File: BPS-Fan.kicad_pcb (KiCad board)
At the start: 2 copper layers, 57.3 x 82.1 mm, 37 parts, among them J1 LDRBRDConn, J10 FAN9, J11 FAN10, J12 FAN11, J13 FAN12, J2 FAN1, J3 FAN2, J4 FAN3, J5 FAN4, J6 FAN5, J7 FAN6, J8 FAN7, J9 FAN8, Q1 BUK9M23-80E, Q2 BUK9M23-80E, Q3 BUK9M23-80E, Q4 BUK9M23-80E

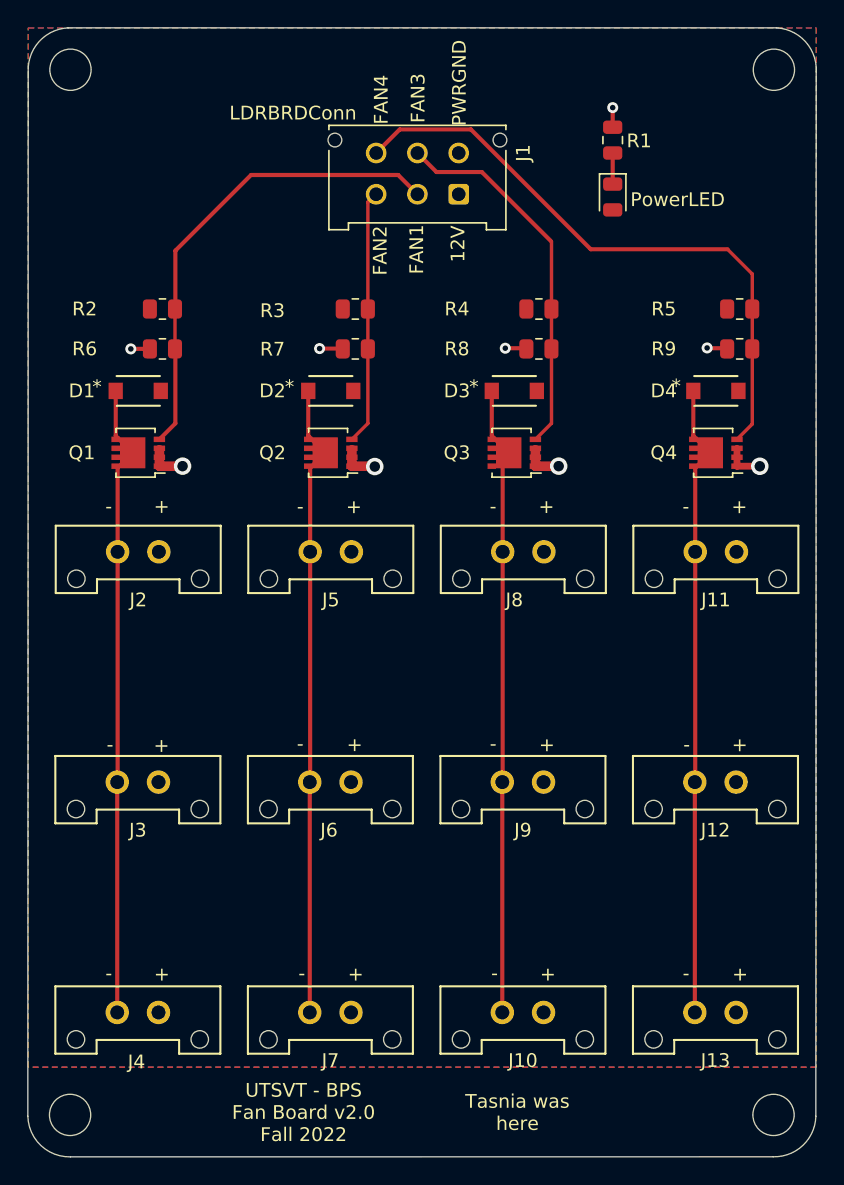
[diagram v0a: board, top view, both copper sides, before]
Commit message: updated BOM and data sheet in schematic
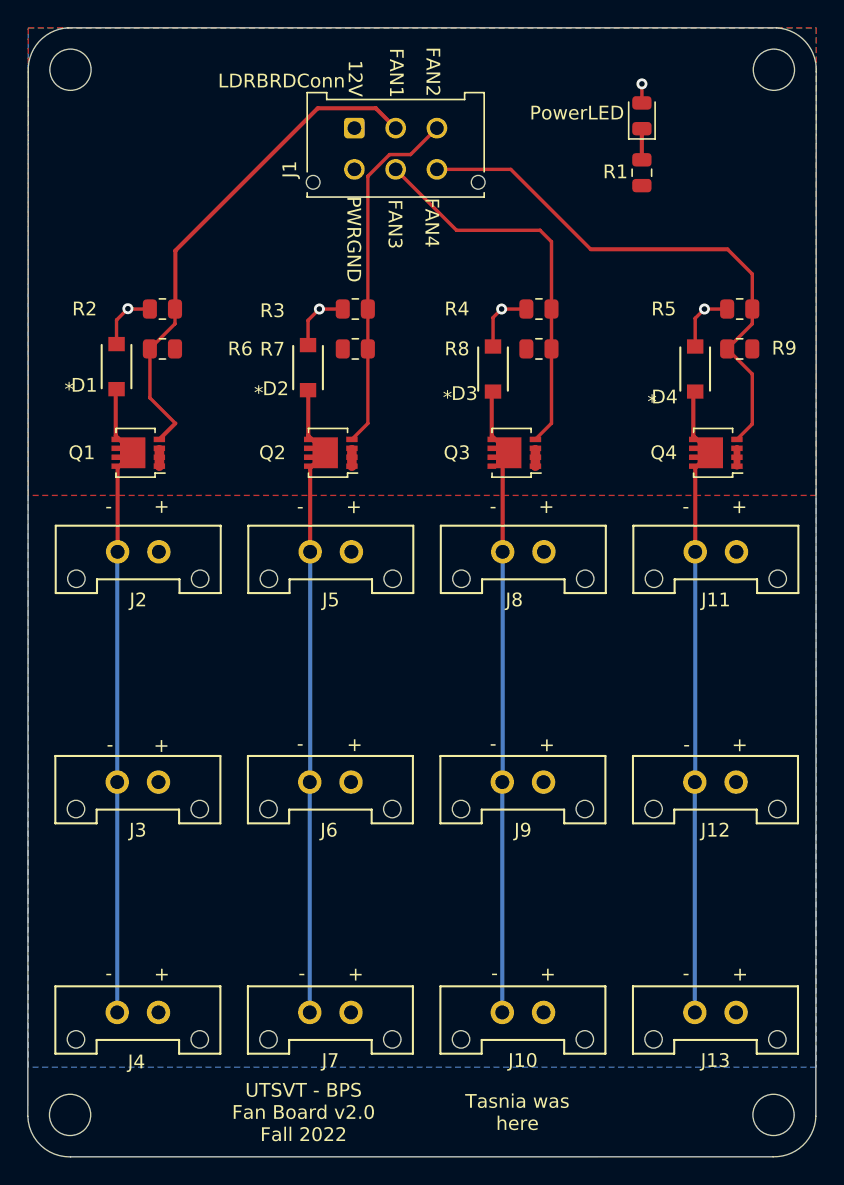
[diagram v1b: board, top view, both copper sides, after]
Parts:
- moved J1 8.98 mm to (152.2, 48.0), turned to 0 degrees
- moved PowerLED 6.27 mm to (173.1, 47.1), turned to 90 degrees
- moved R1 3.18 mm to (173.1, 51.2), turned to -90 degrees
- moved D1 2.37 mm to (134.9, 65.3), turned to -90 degrees
- moved D2 2.37 mm to (148.8, 65.4), turned to -90 degrees
- moved D3 2.22 mm to (162.3, 65.5), turned to -90 degrees
- moved D4 2.19 mm to (177.0, 65.5), turned to -90 degrees
- turned R6 to 0 degrees
- turned R9 to 0 degrees
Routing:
- net +12V: track 0.00 -> 20.0 mm, vias 0 -> 5
- net GNDPWR: track 19.1 -> 4.90 mm, vias 9 -> 0
- net /FAN2_BPS: track 18.6 -> 26.2 mm
- net /FAN4_BPS: track 44.9 -> 40.1 mm
- net /FAN1_BPS: track 34.6 -> 37.1 mm
- net /FAN3_BPS: track 27.3 -> 28.4 mm
- added copper zone on B.Cu, net +12V
- added copper zone on F.Cu, net GNDPWR
- removed copper zone on F.Cu, net +12V
- removed copper zone on B.Cu, net GNDPWR
